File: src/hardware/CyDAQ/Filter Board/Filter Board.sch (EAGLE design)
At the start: 212 parts, among them J1 DCJ0202, J10 Vout_HEADER, J11 5V0_SENSOR, J12 3V3_SENSOR, J13 1V8_SENSOR, J14 BRKOUT_JD, J15 BRKOUT_JC, J16 BRKOUT_JB, J17 BRKOUT_JF, J18 5V0_CONN, J19 3V3_CONN, J2 ZYBO_JF, J20 1V8_CONN, J21 BRKOUT_JD, J3 ZYBO_JE, J4 ZYBO_JD, J5 ZYBO_JC, J6 ZYBO_JB, J7 A_XADC, J8 SJ1-3523N, J9 Vin_HEADER, U1 TPS54531DDARDDA8_3P1X2P4-L, U10 CD74HCT4051, U11 CD74HCT4051, U12 OPA4197, U13 OPA4197, U14 OPA4197, U15 OPA4197, U16 OPA4197, U17 CD74HCT4053, U18 CD74HCT4051, U19 OPA2197, U2 VS-50WQ04FNPBFDPAK-L, U3 TPS56339, U4 TPS56339, U5 LM43601PWPR, U6 X9258_A, U7 X925_B, U8 X9258_C, U9 X9258_D

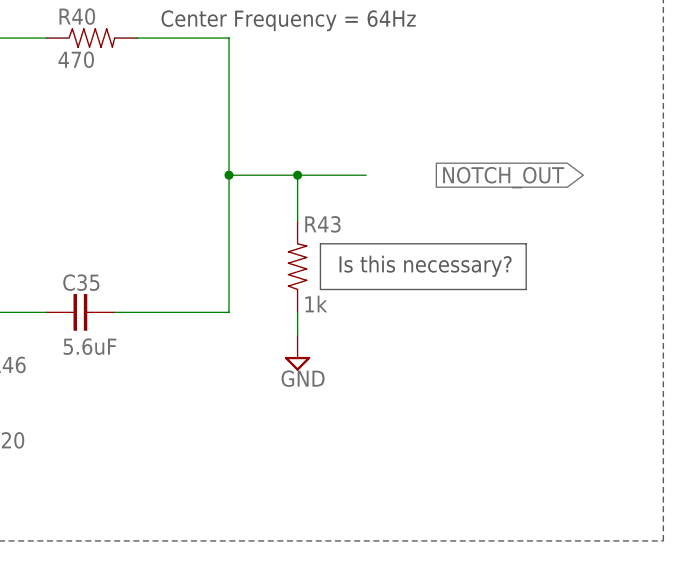
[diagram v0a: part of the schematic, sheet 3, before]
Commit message: Finished most routing. Need to do -5v rail
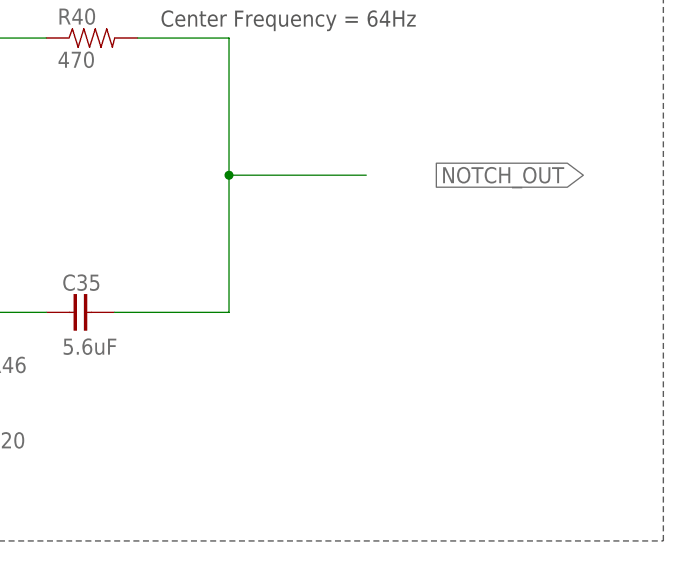
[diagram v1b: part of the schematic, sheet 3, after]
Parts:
- removed R13: 100k, Resistors:SMD_0805
- removed R43: 1k, Resistors:SMD_0805
- R14, R15: value 1.5k -> 4.7k
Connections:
- net 1V8 renamed +1V8
- removed net 3V3: 3V3.TP, C10.1, C50.1, C52.1, C56.1, C58.1, J12.2, J14.1, J14.2, J15.1, J15.2, J16.1, J16.2, J17.1, J17.2, J21.1, J21.2, L2.1, R5.2, U6_MAIN.VCC, U7_MAIN.VCC, U8_MAIN.VCC, U9_MAIN.VCC
- removed net 5V0: C16.1, C17.1, C22.1, C23.1, C24.1, C25.1, C30.1, C51.1, C55.1, C57.1, C6.1, C61.1, C63.1, C65.1, C67.1, C69.1, C72.1, D1.C, G3.TP, J11.2, J18.1, J18.3, J18.5, L1.1, R14.2, R15.2, R16.2, R17.2, R19.2, R2.2, R21.2, R23.2, R25.2, R27.2, R30.2, R32.2, R34.2, R36.2, R67.2, R69.2, R71.2, R73.2, R75.2, R77.2, R81.2, U10.VCC, U11.VCC, U12_P.V+, U13_P.V+, U14_P.V+, U15_P.V+, U16_P.V+, U17.VCC, U18.VCC, U19_P.V+, U5.EN, U5.VIN, U5.VIN_2, U6_MAIN.V+, U7_MAIN.V+, U8_MAIN.V+, U9_MAIN.V+
- new net +5V0: C16.1, C17.1, C22.1, C23.1, C24.1, C25.1, C30.1, C51.1, C55.1, C57.1, C6.1, C61.1, C63.1, C65.1, C67.1, C69.1, C72.1, D1.C, G3.TP, J11.2, J18.1, J18.3, J18.5, L1.1, R16.2, R17.2, R19.2, R2.2, R21.2, R23.2, R25.2, R27.2, R30.2, R32.2, R34.2, R36.2, R67.2, R69.2, R71.2, R73.2, R75.2, R77.2, R81.2, U10.VCC, U11.VCC, U12_P.V+, U13_P.V+, U14_P.V+, U15_P.V+, U16_P.V+, U17.VCC, U18.VCC, U19_P.V+, U5.EN, U5.VIN, U5.VIN_2, U6_MAIN.V+, U7_MAIN.V+, U8_MAIN.V+, U9_MAIN.V+
- net !SYSTEM_EN: no longer R13.2
- net +3V3: now also 3V3.TP, C10.1, C50.1, C52.1, C56.1, C58.1, J12.2, J14.1, J14.2, J15.1, J15.2, J16.1, J16.2, J17.1, J17.2, J21.1, J21.2, L2.1, R14.2, R15.2, R5.2, U6_MAIN.VCC, U7_MAIN.VCC, U8_MAIN.VCC, U9_MAIN.VCC
- net GND: no longer R13.1, R43.1
- net NOTCH_OUT: no longer R43.2
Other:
- note removed: "Is this necessary?"

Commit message: Finished routing and made mechanical adjustments
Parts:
- added J22: ZYBO_Power, SparkFun-Connectors:CONN_02LOCK
- renumbered U2 to D3
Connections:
- new net +5V: J22.2
- net +5V0: now also +5V.TP; no longer G3.TP
- net GND: now also G3.TP, J22.1; no longer +5V.TP
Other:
- moved on the sheet: +5V, G3
